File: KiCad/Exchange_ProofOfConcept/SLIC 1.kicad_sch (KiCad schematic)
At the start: 9 parts

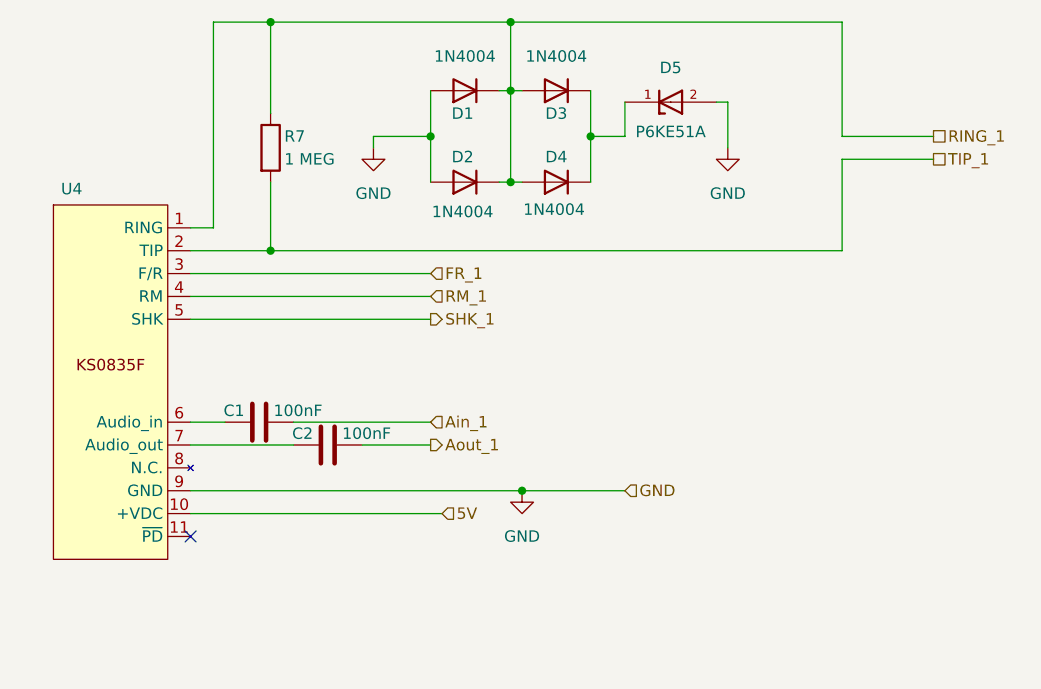
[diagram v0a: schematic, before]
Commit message: deleted:    KiCad/Exchange_ProofOfConcept/Exchange_ProofOfConcept-backups/Exchange_ProofOfConcept-2024-08-28_233227.zip 	deleted:    KiCad/Exchange_ProofOfConcept/Exchange_ProofOfConcept-backups/Exchange_ProofOfConcept-2024-08-28_234504.zip 	deleted:    KiCad/Exchange_ProofOfConcept/Exchange_ProofOfConcept-backups/Exchange_ProofOfConcept-2024-09-04_201626.zip 	deleted:    KiCad/Exchange_ProofOfConcept/Exchange_ProofOfConcept-backups/Exchange_ProofOfConcept-2024-09-04_202659.zip 	deleted:    KiCad/Exchange_ProofOfConcept/Exchange_ProofOfConcept-backups/Exchange_ProofOfConcept-2024-09-04_203703.zip 	deleted:    KiCad/Exchange_ProofOfConcept/Exchange_ProofOfConcept-backups/Exchange_ProofOfConcept-2024-09-04_204710.zip 	deleted:    KiCad/Exchange_ProofOfConcept/Exchange_ProofOfConcept-backups/Exchange_ProofOfConcept-2024-09-04_205754.zip 	deleted:    KiCad/Exchange_ProofOfConcept/Exchange_ProofOfConcept-backups/Exchange_ProofOfConcept-2024-09-05_153643.zip 	deleted:    KiCad/Exchange_ProofOfConcept/Exchange_ProofOfConcept-backups/Exchange_ProofOfConcept-2024-09-05_161017.zip 	deleted:    KiCad/Exchange_ProofOfConcept/Exchange_ProofOfConcept-backups/Exchange_ProofOfConcept-2024-09-05_162441.zip 	deleted:    KiCad/Exchange_ProofOfConcept/Exchange_ProofOfConcept-backups/Exchange_ProofOfConcept-2024-09-05_163641.zip 	deleted:    KiCad/Exchange_ProofOfConcept/Exchange_ProofOfConcept-backups/Exchange_ProofOfConcept-2024-09-06_180233.zip 	deleted:    KiCad/Exchange_ProofOfConcept/Exchange_ProofOfConcept-backups/Exchange_ProofOfConcept-2024-09-06_180943.zip 	deleted:    KiCad/Exchange_ProofOfConcept/Exchange_ProofOfConcept-backups/Exchange_ProofOfConcept-2024-09-06_182256.zip 	deleted:    KiCad/Exchange_ProofOfConcept/Exchange_ProofOfConcept-backups/Exchange_ProofOfConcept-2024-09-06_185314.zip 	deleted:    KiCad/Exchange_ProofOfConcept/Exchange_ProofOfConcept-backups/Exchange_ProofOfConcept-2024-09-06_191143.zip 	deleted:    KiCad/Exchange_ProofOfConcept/Exchange_ProofOfConcep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
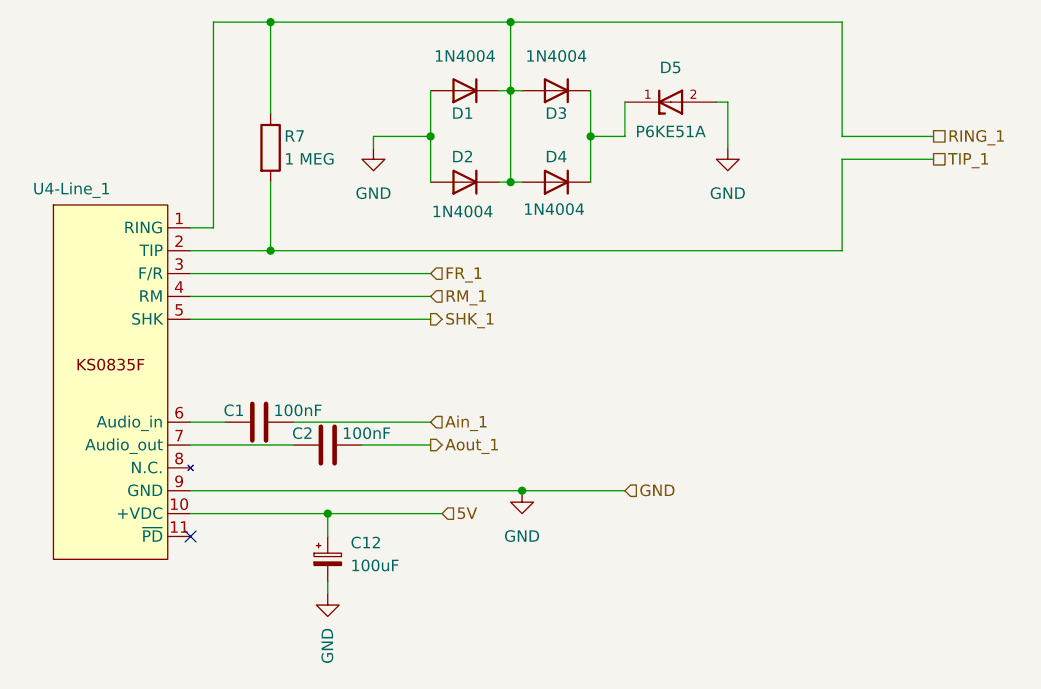
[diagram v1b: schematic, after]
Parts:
- added C12: 100uF, Capacitor_THT:CP_Radial_D5.0mm_P2.00mm, symbol Device:C_Polarized_Small
- renumbered U4 to U4-Line_1
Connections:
- net 5V: now also C12.1
- net GND: now also C12.2
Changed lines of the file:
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@@
+		(color 0 0 0 0)
+	)
+	(junction
+		(at 66.04 91.44)
+		(diameter 0)
 		(color 0 0 0 0)
 	)
@@
 	(wire
 		(pts
+			(xy 66.04 93.98) (xy 66.04 91.44)
+		)
+		(stroke
+			(width 0)
+			(type default)
+		)
+	)
+	(wire
+		(pts
 			(xy 86.36 36.83) (xy 86.36 44.45)
 		)
@@
 	(wire
 		(pts
+			(xy 66.04 91.44) (xy 78.74 91.44)
+		)
+		(stroke
+			(width 0)
+			(type default)
+		)
+	)
+	(wire
+		(pts
 			(xy 86.36 44.45) (xy 86.36 54.61)
 		)
@@
 	(wire
 		(pts
-			(xy 50.8 91.44) (xy 78.74 91.44)
+			(xy 50.8 91.44) (xy 66.04 91.44)
 		)
 		(stroke
@@
 		(pts
 			(xy 99.06 45.72) (xy 99.06 49.53)
+		)
+		(stroke
+			(width 0)
+			(type default)
+		)
+	)
+	(wire
+		(pts
+			(xy 66.04 99.06) (xy 66.04 100.33)
 		)
 		(stroke
@@
 		(on_board yes)
 		(dnp no)
-		(property "Reference" "U4"
+		(property "Reference" "U4-Line_1"
 			(at 37.592 55.372 0)
 			(effects
@@
 			(project "Exchange_ProofOfConcept"
 				(path "/a3aa82f3-37b8-406c-999a-d11513c8e1fa/9d9e2000-7f80-467e-a3ef-e363659fc38e"
-					(reference "U4")
+					(reference "U4-Line_1")
 					(unit 1)
 				)
@@
 				(path "/a3aa82f3-37b8-406c-999a-d11513c8e1fa/9d9e2000-7f80-467e-a3ef-e363659fc38e"
 					(reference "C2")
+					(unit 1)
+				)
+			)
+		)
+	)
+	(symbol
+		(lib_id "Device:C_Polarized_Small")
+		(at 66.04 96.52 0)
+		(unit 1)
+		(exclude_from_sim no)
+		(in_bom yes)
+		(on_board yes)
+		(dnp no)
+		(fields_autoplaced yes)
+		(property "Reference" "C12"
+			(at 68.58 94.7038 0)
+			(effects
+				(font
+					(size 1.27 1.27)
+				)
+				(justify left)
+			)
+		)
+		(property "Value" "100uF"
+			(at 68.58 97.2438 0)
+			(effects
+				(font
+					(size 1.27 1.27)
+				)
+				(justify left)
+			)
+		)
+		(property "Footprint" "Capacitor_THT:CP_Radial_D5.0mm_P2.00mm"
+			(at 66.04 96.52 0)
+			(effects
+				(font
+					(size 1.27 1.27)
+				)
+				(hide yes)
+			)
+		)
+		(property "Datasheet" "~"
+			(at 66.04 96.52 0)
+			(effects
+				(font
+					(size 1.27 1.27)
+				)
+				(hide yes)
+			)
+		)
+		(property "Description" "Polarized capacitor, small symbol"
+			(at 66.04 96.52 0)
+			(effects
+				(font
+					(size 1.27 1.27)
+				)
+				(hide yes)
+			)
+		)
+		(pin "1"
+		)
+		(pin "2"
+		)
+		(instances
+			(project "Exchange_ProofOfConcept"
+				(path "/a3aa82f3-37b8-406c-999a-d11513c8e1fa/9d9e2000-7f80-467e-a3ef-e363659fc38e"
+					(reference "C12")
 					(unit 1)
 				)
@@
 					(unit 1)
 				)
+			)
+		)
+	)
+	(symbol
+		(lib_id "power:GND")
+		(at 66.04 100.33 0)
+		(unit 1)
+		(exclude_from_sim no)
+		(in_bom yes)
+		(on_board yes)
+		(dnp no)
+		(fields_autoplaced yes)
+		(property "Reference" "#PWR011"
+			(at 66.04 106.68 0)
+			(effects
+				(font
+					(size 1.27 1.27)
+				)
+				(hide yes)
+			)
+		)
+		(property "Value" "GND"
+			(at 66.0401 104.14 90)
+			(effects
+				(font
+					(size 1.27 1.27)
+				)
+				(justify right)
+			)
+		)
+		(property "Footprint" ""
+			(at 66.04 100.33 0)
+			(effects
+				(font
+					(size 1.27 1.27)
+				)
+				(hide yes)
+			)
+		)
+		(property "Datasheet" ""
+			(at 66.04 100.33 0)
+			(effects
+				(font
+					(size 1.27 1.27)
+				)
+				(hide yes)
+			)
+		)
+		(property "Description" "Power symbol creates a global label with name \"GND\" , ground"
+			(at 66.04 100.33 0)
+			(effects
+				(font
+					(size 1.27 1.27)
+				)
+				(hide yes)
+			)
+		)
+		(pin "1"
+		)
+		(instances
+			(project "Exchange_ProofOfConcept"
+				(path "/a3aa82f3-37b8-406c-999a-d11513c8e1fa/9d9e2000-7f80-467e-a3ef-e363659fc38e"
+					(reference "#PWR011")
+					(unit 1)
+				)

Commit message: new file:   KiCad/Exchange_ProofOfConcept/ESP-Unit/ESP-Unit-backups/ESP-Unit-2024-10-22_204833.zip 	new file:   KiCad/Exchange_ProofOfConcept/ESP-Unit/ESP-Unit-backups/ESP-Unit-2024-10-22_205851.zip 	new file:   KiCad/Exchange_ProofOfConcept/ESP-Unit/ESP-Unit-backups/ESP-Unit-2024-10-22_214835.zip 	new file:   KiCad/Exchange_ProofOfConcept/ESP-Unit/ESP-Unit-backups/ESP-Unit-2024-10-31_190638.zip 	new file:   KiCad/Exchange_ProofOfConcept/ESP-Unit/ESP-Unit.kicad_pcb 	new file:   KiCad/Exchange_ProofOfConcept/ESP-Unit/ESP-Unit.kicad_prl 	new file:   KiCad/Exchange_ProofOfConcept/ESP-Unit/ESP-Unit.kicad_pro 	new file:   KiCad/Exchange_ProofOfConcept/ESP-Unit/ESP-Unit.kicad_sch 	new file:   KiCad/Exchange_ProofOfConcept/ESP-Unit/fp-info-cache 	deleted:    KiCad/Exchange_ProofOfConcept/Exchange_ProofOfConcept-backups/Exchange_ProofOfConcept-2024-09-09_193050.zip 	deleted:    KiCad/Exchange_ProofOfConcept/Exchange_ProofOfConcept-backups/Exchange_ProofOfConcept-2024-09-10_220108.zip 	deleted:    KiCad/Exchange_ProofOfConcept/Exchange_ProofOfConcept-backups/Exchange_ProofOfConcept-2024-09-10_232037.zip 	deleted:    KiCad/Exchange_ProofOfConcept/Exchange_ProofOfConcept-backups/Exchange_ProofOfConcept-2024-09-11_034329.zip 	deleted:    KiCad/Exchange_ProofOfConcept/Exchange_ProofOfConcept-backups/Exchange_ProofOfConcept-2024-09-11_195456.zip 	deleted:    KiCad/Exchange_ProofOfConcept/Exchange_ProofOfConcept-backups/Exchange_ProofOfConcept-2024-09-17_174014.zip 	deleted:    KiCad/Exchange_ProofOfConcept/Exchange_ProofOfConcept-backups/Exchange_ProofOfConcept-2024-09-17_181112.zip 	deleted:    KiCad/Exchange_ProofOfConcept/Exchange_ProofOfConcept-backups/Exchange_ProofOfConcept-2024-09-19_202603.zip 	deleted:    KiCad/Exchange_ProofOfConcept/Exchange_ProofOfConcept-backups/Exchange_ProofOfConcept-2024-09-19_204637.zip 	deleted:    KiCad/Exchange_ProofOfConcept/Exchange_ProofOfConcept-backups/Exchange_ProofOfConcept-2024-09-19_205646.zip 	deleted:    KiCad/Exchange_ProofOfConcep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
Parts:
- R7: footprint Resistor_THT:R_Axial_DIN0204_L3.6mm_D1.6mm_P5.08mm_Horizontal -> Resistor_THT:R_Axial_DIN0207_L6.3mm_D2.5mm_P7.62mm_Horizontal
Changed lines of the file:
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@@
 			)
 		)
-		(property "Footprint" "Resistor_THT:R_Axial_DIN0204_L3.6mm_D1.6mm_P5.08mm_Horizontal"
+		(property "Footprint" "Resistor_THT:R_Axial_DIN0207_L6.3mm_D2.5mm_P7.62mm_Horizontal"
 			(at 57.912 50.8 90)
 			(effects

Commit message: deleted:    KiCad/Exchange_ProofOfConcept/Exchange_ProofOfConcept-backups/Exchange_ProofOfConcept-2024-09-22_005800.zip 	deleted:    KiCad/Exchange_ProofOfConcept/Exchange_ProofOfConcept-backups/Exchange_ProofOfConcept-2024-09-22_010415.zip 	deleted:    KiCad/Exchange_ProofOfConcept/Exchange_ProofOfConcept-backups/Exchange_ProofOfConcept-2024-09-22_093037.zip 	deleted:    KiCad/Exchange_ProofOfConcept/Exchange_ProofOfConcept-backups/Exchange_ProofOfConcept-2024-09-22_093847.zip 	deleted:    KiCad/Exchange_ProofOfConcept/Exchange_ProofOfConcept-backups/Exchange_ProofOfConcept-2024-09-22_094927.zip 	deleted:    KiCad/Exchange_ProofOfConcept/Exchange_ProofOfConcept-backups/Exchange_ProofOfConcept-2024-10-02_184119.zip 	deleted:    KiCad/Exchange_ProofOfConcept/Exchange_ProofOfConcept-backups/Exchange_ProofOfConcept-2024-10-06_223658.zip 	new file:   KiCad/Exchange_ProofOfConcept/Exchange_ProofOfConcept-backups/Exchange_ProofOfConcept-2024-11-20_223020.zip 	new file:   KiCad/Exchange_ProofOfConcept/Exchange_ProofOfConcept-backups/Exchange_ProofOfConcept-2024-11-20_223933.zip 	new file:   KiCad/Exchange_ProofOfConcept/Exchange_ProofOfConcept-backups/Exchange_ProofOfConcept-2024-11-20_224852.zip 	new file:   KiCad/Exchange_ProofOfConcept/Exchange_ProofOfConcept-backups/Exchange_ProofOfConcept-2024-11-20_230009.zip 	new file:   KiCad/Exchange_ProofOfConcept/Exchange_ProofOfConcept-backups/Exchange_ProofOfConcept-2024-11-20_231023.zip 	new file:   KiCad/Exchange_ProofOfConcept/Exchange_ProofOfConcept-backups/Exchange_ProofOfConcept-2024-11-20_231736.zip 	modified:   KiCad/Exchange_ProofOfConcept/Exchange_ProofOfConcept.kicad_pcb 	modified:   KiCad/Exchange_ProofOfConcept/Exchange_ProofOfConcept.kicad_prl 	modified:   KiCad/Exchange_ProofOfConcept/Exchange_ProofOfConcept.kicad_pro 	modified:   KiCad/Exchange_ProofOfConcept/Exchange_ProofOfConcept.kicad_sch 	modified:   KiCad/Exchange_ProofOfConcept/SLIC 1.kicad_sch 	modified:   KiCad/Exchange_ProofOfConcept/SLIC 1_sch.kicad_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
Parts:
- R7: footprint Resistor_THT:R_Axial_DIN0207_L6.3mm_D2.5mm_P7.62mm_Horizontal -> Resistor_THT:R_Axial_DIN0207_L6.3mm_D2.5mm_P2.54mm_Vertical
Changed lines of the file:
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@@
 			)
 		)
-		(property "Footprint" "Resistor_THT:R_Axial_DIN0207_L6.3mm_D2.5mm_P7.62mm_Horizontal"
+		(property "Footprint" "Resistor_THT:R_Axial_DIN0207_L6.3mm_D2.5mm_P2.54mm_Vertical"
 			(at 57.912 50.8 90)
 			(effects
